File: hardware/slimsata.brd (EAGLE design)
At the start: 16.9 x 80 mm, 2 parts

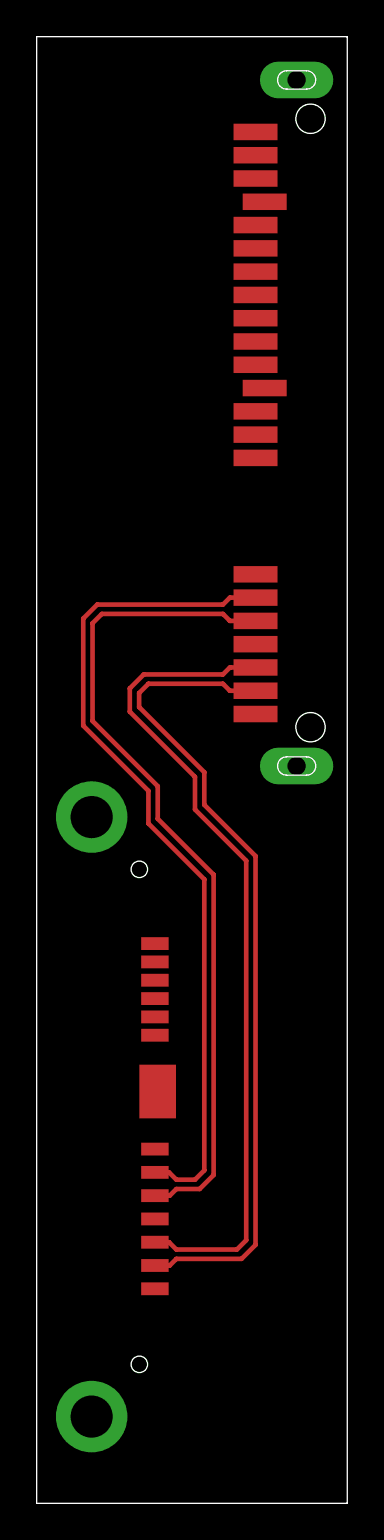
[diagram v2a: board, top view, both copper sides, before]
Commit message: Massefläche eingefügt
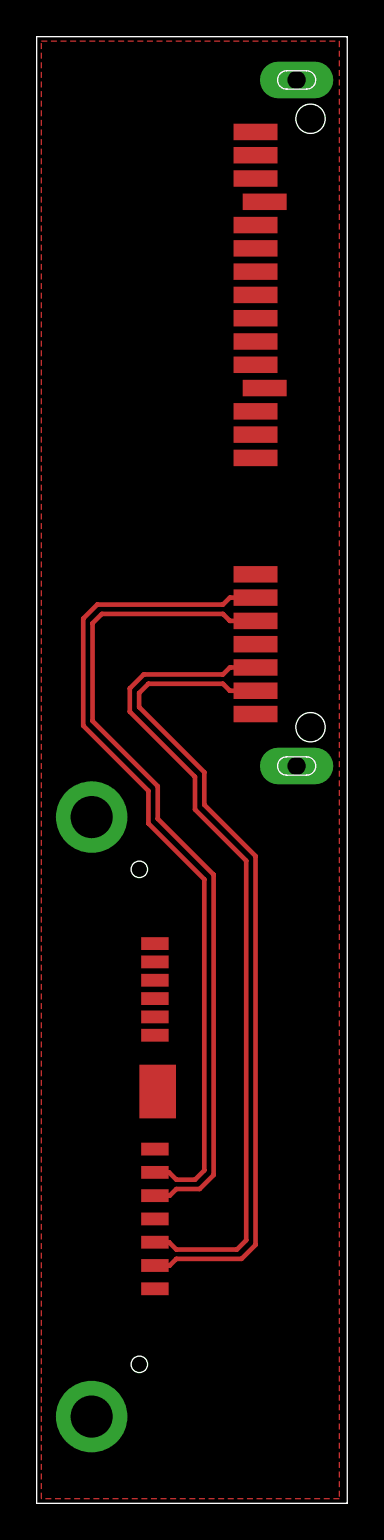
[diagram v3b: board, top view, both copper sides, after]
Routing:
- added copper zone on layer 1, net GND
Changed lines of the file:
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@@
 <setting verticaltext="up"/>
 </settings>
-<grid distance="5" unitdist="mil" unit="mil" style="dots" multiple="1" display="yes" altdistance="0.025" altunitdist="inch" altunit="inch"/>
+<grid distance="10" unitdist="mil" unit="mil" style="dots" multiple="1" display="yes" altdistance="0.025" altunitdist="inch" altunit="inch"/>
 <layers>
 <layer number="1" name="Top" color="4" fill="1" visible="yes" active="yes"/>
@@
 </class>
 </classes>
-<designrules name="default">
-<description language="de">&lt;b&gt;EAGLE Design Rules&lt;/b&gt;
-&lt;p&gt;
-Die Standard-Design-Rules sind so gewählt, dass sie für
-die meisten Anwendungen passen. Sollte ihre Platine
-besondere Anforderungen haben, treffen Sie die erforderlichen
-Einstellungen hier und speichern die Design Rules unter
-einem neuen Namen ab.</description>
+<designrules name="platinensammler_02_mod">
+<description language="de">&lt;b&gt; DRC-File für Sammelnutzen. &lt;/b&gt;&lt;br&gt;&lt;br&gt;
+Die in diesen Designregeln festgelegten Maße, Abstände und Durchmesser stellen die Mindestanforderungen für eine Teilnahme am Sammelnutzen dar und lauten wie folgt:&lt;br&gt;&lt;br&gt;
+&lt;table border=1&gt;
+&lt;tr&gt;
+&lt;th&gt;Bezeichnung&lt;/th&gt;
+&lt;th&gt;Maß&lt;/th&gt;
+&lt;/tr&gt;
+&lt;tr&gt;
+&lt;td&gt;min. Leiterbahnenbreite &lt;/td&gt;
+&lt;td&gt;0,15mm&lt;/td&gt;
+&lt;/tr&gt;
+&lt;tr&gt;
+&lt;td&gt;min. Leiterbahnenabstand &lt;/td&gt;
+&lt;td&gt;0,15mm&lt;/td&gt;
+&lt;/tr&gt;
+&lt;tr&gt;
+&lt;td&gt;min. Abstand Kupfer zu Kontur   &lt;/td&gt;
+&lt;td&gt;0,2mm&lt;/td&gt;
+&lt;/tr&gt;
+&lt;tr&gt;
+&lt;td&gt;&lt;/td&gt;
+&lt;td&gt;&lt;/td&gt;
+&lt;/tr&gt;
+&lt;tr&gt;
+&lt;td&gt;min. Bohrdurchmesser&lt;/td&gt;
+&lt;td&gt;0,3mm&lt;/td&gt;
+&lt;/tr&gt;
+&lt;/table&gt;
+&lt;br&gt;&lt;br&gt;
+Alle Durchkontaktierungen unter 0,8mm gelten als Via und werden abgedeckt.&lt;br&gt; (kann man über &quot;Masks/Limit&quot; verändern)&lt;br&gt;&lt;br&gt;
+Thermals für Vias sind ausgeschaltet (kann man über &quot;Supply/generate thermals for vias&quot; einschalten)&lt;br&gt;&lt;br&gt;
+Natürlich können Sie alle Einstellungen &quot;nach oben&quot; korregieren, wenn Sie dies für Ihr Layout benötigen.&lt;br&gt;&lt;br&gt;
+Sollten Sie Fragen zu den Designregeln haben, können Sie mich über &lt;b&gt;platinensammler@gmail.com&lt;/b&gt; erreichen.&lt;br&gt;&lt;br&gt;
+Jakob Kleinen</description>
 <description language="en">&lt;b&gt;EAGLE Design Rules&lt;/b&gt;
 &lt;p&gt;
@@
 <param name="mtCopper" value="0.035mm 0.035mm 0.035mm 0.035mm 0.035mm 0.035mm 0.035mm 0.035mm 0.035mm 0.035mm 0.035mm 0.035mm 0.035mm 0.035mm 0.035mm 0.035mm"/>
 <param name="mtIsolate" value="1.5mm 0.15mm 0.2mm 0.15mm 0.2mm 0.15mm 0.2mm 0.15mm 0.2mm 0.15mm 0.2mm 0.15mm 0.2mm 0.15mm 0.2mm"/>
-<param name="mdWireWire" value="8mil"/>
-<param name="mdWirePad" value="8mil"/>
-<param name="mdWireVia" value="8mil"/>
-<param name="mdPadPad" value="8mil"/>
-<param name="mdPadVia" value="8mil"/>
-<param name="mdViaVia" value="8mil"/>
-<param name="mdSmdPad" value="8mil"/>
-<param name="mdSmdVia" value="8mil"/>
-<param name="mdSmdSmd" value="8mil"/>
+<param name="mdWireWire" value="0.15mm"/>
+<param name="mdWirePad" value="0.15mm"/>
+<param name="mdWireVia" value="0.15mm"/>
+<param name="mdPadPad" value="0.15mm"/>
+<param name="mdPadVia" value="0.15mm"/>
+<param name="mdViaVia" value="0.15mm"/>
+<param name="mdSmdPad" value="0mil"/>
+<param name="mdSmdVia" value="0mil"/>
+<param name="mdSmdSmd" value="0mil"/>
 <param name="mdViaViaSameLayer" value="8mil"/>
 <param name="mnLayersViaInSmd" value="2"/>
-<param name="mdCopperDimension" value="40mil"/>
-<param name="mdDrill" value="8mil"/>
+<param name="mdCopperDimension" value="0.2mm"/>
+<param name="mdDrill" value="0.2mm"/>
 <param name="mdSmdStop" value="0mil"/>
-<param name="msWidth" value="10mil"/>
-<param name="msDrill" value="24mil"/>
-<param name="msMicroVia" value="9.99mm"/>
+<param name="msWidth" value="0.15mm"/>
+<param name="msDrill" value="0.3mm"/>
+<param name="msMicroVia" value="0.3mm"/>
 <param name="msBlindViaRatio" value="0.5"/>
 <param name="rvPadTop" value="0.25"/>
@@
 <param name="rvMicroViaOuter" value="0.25"/>
 <param name="rvMicroViaInner" value="0.25"/>
-<param name="rlMinPadTop" value="10mil"/>
+<param name="rlMinPadTop" value="0.2mm"/>
 <param name="rlMaxPadTop" value="20mil"/>
-<param name="rlMinPadInner" value="10mil"/>
+<param name="rlMinPadInner" value="0.2mm"/>
 <param name="rlMaxPadInner" value="20mil"/>
-<param name="rlMinPadBottom" value="10mil"/>
+<param name="rlMinPadBottom" value="0.2mm"/>
 <param name="rlMaxPadBottom" value="20mil"/>
-<param name="rlMinViaOuter" value="8mil"/>
+<param name="rlMinViaOuter" value="0.2mm"/>
 <param name="rlMaxViaOuter" value="20mil"/>
-<param name="rlMinViaInner" value="8mil"/>
+<param name="rlMinViaInner" value="0.2mm"/>
 <param name="rlMaxViaInner" value="20mil"/>
-<param name="rlMinMicroViaOuter" value="4mil"/>
+<param name="rlMinMicroViaOuter" value="0.2mm"/>
 <param name="rlMaxMicroViaOuter" value="20mil"/>
-<param name="rlMinMicroViaInner" value="4mil"/>
+<param name="rlMinMicroViaInner" value="0.2mm"/>
 <param name="rlMaxMicroViaInner" value="20mil"/>
 <param name="psTop" value="-1"/>
@@
 <param name="mlMinCreamFrame" value="0mil"/>
 <param name="mlMaxCreamFrame" value="0mil"/>
-<param name="mlViaStopLimit" value="0mil"/>
+<param name="mlViaStopLimit" value="0.8mm"/>
 <param name="srRoundness" value="0"/>
 <param name="srMinRoundness" value="0mil"/>
 <param name="srMaxRoundness" value="0mil"/>
-<param name="slThermalIsolate" value="10mil"/>
+<param name="slThermalIsolate" value="0.15mm"/>
 <param name="slThermalsForVias" value="0"/>
 <param name="dpMaxLengthDifference" value="10mm"/>
 <param name="dpGapFactor" value="2.5"/>
 <param name="checkGrid" value="0"/>
-<param name="checkAngle" value="0"/>
+<param name="checkAngle" value="1"/>
 <param name="checkFont" value="1"/>
 <param name="checkRestrict" value="1"/>
@@
 <wire x1="11.938" y1="35.306" x2="9.144" y2="38.1" width="0.254" layer="1"/>
 <wire x1="5.588" y1="44.196" x2="5.588" y2="43.434" width="0.254" layer="1"/>
-<wire x1="5.588" y1="43.434" x2="9.144" y2="39.878" width="0.254" layer="1"/>
+<wire x1="9.144" y1="39.878" x2="5.588" y2="43.434" width="0.254" layer="1"/>
 <wire x1="9.144" y1="39.878" x2="9.144" y2="38.1" width="0.254" layer="1"/>
 <wire x1="11.938" y1="44.323" x2="10.541" y2="44.323" width="0.254" layer="1"/>
@@
 <wire x1="11.43" y1="14.351" x2="11.43" y2="35.052" width="0.254" layer="1"/>
 <wire x1="11.43" y1="35.052" x2="8.636" y2="37.846" width="0.254" layer="1"/>
-<wire x1="5.08" y1="44.45" x2="5.08" y2="43.18" width="0.254" layer="1"/>
+<wire x1="5.08" y1="43.18" x2="5.08" y2="44.45" width="0.254" layer="1"/>
 <wire x1="5.08" y1="43.18" x2="8.636" y2="39.624" width="0.254" layer="1"/>
 <wire x1="8.636" y1="39.624" x2="8.636" y2="37.846" width="0.254" layer="1"/>
@@
 <wire x1="7.62" y1="17.145" x2="8.89" y2="17.145" width="0.254" layer="1"/>
 <wire x1="8.89" y1="17.145" x2="9.652" y2="17.907" width="0.254" layer="1"/>
-<wire x1="9.652" y1="17.907" x2="9.652" y2="34.29" width="0.254" layer="1"/>
+<wire x1="9.652" y1="34.29" x2="9.652" y2="17.907" width="0.254" layer="1"/>
 <wire x1="9.652" y1="34.29" x2="6.604" y2="37.338" width="0.254" layer="1"/>
 <wire x1="3.556" y1="48.514" x2="3.048" y2="48.006" width="0.254" layer="1"/>
-<wire x1="3.048" y1="48.006" x2="3.048" y2="42.672" width="0.254" layer="1"/>
+<wire x1="3.048" y1="42.672" x2="3.048" y2="48.006" width="0.254" layer="1"/>
 <wire x1="3.048" y1="42.672" x2="6.604" y2="39.116" width="0.254" layer="1"/>
 <wire x1="6.604" y1="39.116" x2="6.604" y2="37.338" width="0.254" layer="1"/>
@@
 <wire x1="7.62" y1="17.653" x2="8.636" y2="17.653" width="0.254" layer="1"/>
 <wire x1="8.636" y1="17.653" x2="9.144" y2="18.161" width="0.254" layer="1"/>
-<wire x1="9.144" y1="18.161" x2="9.144" y2="34.036" width="0.254" layer="1"/>
+<wire x1="9.144" y1="34.036" x2="9.144" y2="18.161" width="0.254" layer="1"/>
 <wire x1="9.144" y1="34.036" x2="6.096" y2="37.084" width="0.254" layer="1"/>
 <wire x1="3.302" y1="49.022" x2="2.54" y2="48.26" width="0.254" layer="1"/>
@@
 <contactref element="CON2" pad="P6"/>
 <contactref element="CON2" pad="P5"/>
+<polygon width="0.4064" layer="1">
+<vertex x="0.254" y="79.756"/>
+<vertex x="16.51" y="79.756"/>
+<vertex x="16.51" y="0.254"/>
+<vertex x="0.254" y="0.254"/>
+</polygon>
 <wire x1="12.438" y1="70.993" x2="14.178" y2="77.638" width="0" layer="19" extent="1-1"/>
+<wire x1="11.938" y1="68.453" x2="12.438" y2="70.993" width="0" layer="19" extent="1-1"/>
+<wire x1="11.938" y1="63.373" x2="11.938" y2="68.453" width="0" layer="19" extent="1-1"/>
+<wire x1="11.938" y1="62.103" x2="11.938" y2="63.373" width="0" layer="19" extent="1-1"/>
+<wire x1="12.438" y1="60.833" x2="11.938" y2="62.103" width="0" layer="19" extent="1-1"/>
+<wire x1="11.938" y1="50.673" x2="12.438" y2="60.833" width="0" layer="19" extent="1-1"/>
+<wire x1="11.938" y1="46.863" x2="11.938" y2="50.673" width="0" layer="19" extent="1-1"/>
+<wire x1="11.938" y1="43.053" x2="11.938" y2="46.863" width="0" layer="19" extent="1-1"/>
 <wire x1="14.178" y1="40.218" x2="11.938" y2="43.053" width="0" layer="19" extent="1-1"/>
+<wire x1="3" y1="37.432" x2="11.938" y2="43.053" width="0" layer="19" extent="1-1"/>
+<wire x1="6.45" y1="30.532" x2="3" y2="37.432" width="0" layer="19" extent="1-1"/>
+<wire x1="6.45" y1="29.532" x2="6.45" y2="30.532" width="0" layer="19" extent="1-1"/>
+<wire x1="6.6" y1="22.462" x2="6.45" y2="29.532" width="0" layer="19" extent="1-1"/>
+<wire x1="6.45" y1="19.322" x2="6.6" y2="22.462" width="0" layer="19" extent="1-1"/>
+<wire x1="6.45" y1="15.512" x2="6.45" y2="19.322" width="0" layer="19" extent="1-1"/>
+<wire x1="6.45" y1="11.702" x2="6.45" y2="15.512" width="0" layer="19" extent="1-1"/>
+<wire x1="3" y1="4.732" x2="6.45" y2="11.702" width="0" layer="19" extent="1-1"/>
 </signal>
 </signals>
